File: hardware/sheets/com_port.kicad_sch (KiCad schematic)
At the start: 19 parts, among them J1 DE9_Pins, J2 Conn_01x03, J3 Conn_01x04, U1 16550, U2 MAX3241, U3 74HCT04, U4 74HCT08, U5 74HCT08, U6 74HCT125, Y1 1.8432MHz

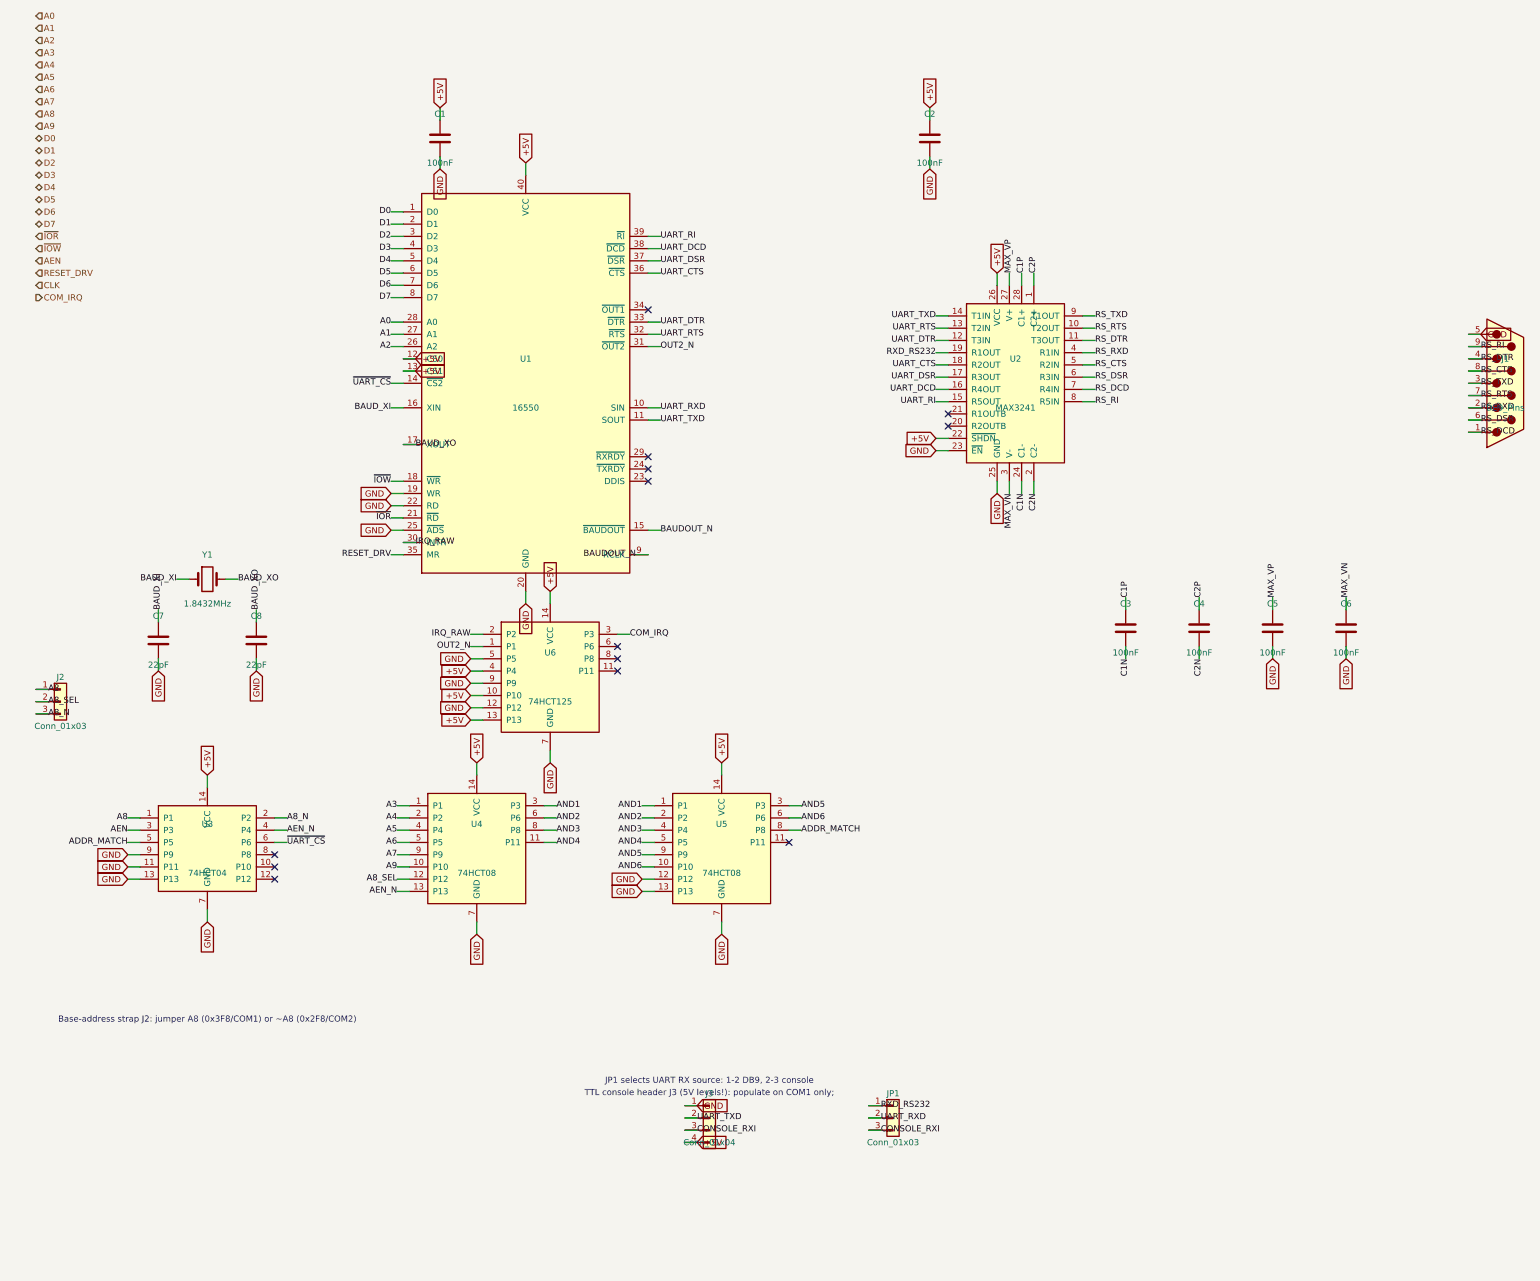
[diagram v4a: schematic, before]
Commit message: Design review 2026-07-11: rail protection, decoupling, wiring fixes
Protection:
- Sidecar +5V now feeds through a 2A polyfuse into +5V_ISA with an
  SMBJ5.0A clamp + 22uF bulk (a faulted ISA card trips its own fuse
  instead of dropping the board; back-fed voltage is clamped).
- USB-C VBUS enters through a 3A polyfuse with an SMBJ5.0A on +5V
  (backstop for the CFG1 9-20V failure mode). CH224K gains a 1uF VDD
  cap; its PG routes to Supervisor GPIO16 as PD_PG. Buck output
  doubled to 2x22uF, 10uF at VIN, extra rail bulk.
- Supervisor USB-A host port: 27R series termination (RP2040
  requirement), USBLC6-2SC6 ESD array, 100uF VBUS bulk.
- Video: HDMI +5V fused (500mA), HPD sensed on GPIO41, 100R series on
  VGA sync. TMDS ESD array deferred to layout (no symbol).
- card_isatest: V5RAW bulk, Q1 gate soft-start cap, TVS on DUT rail.

Wiring fixes:
- SPKR had no driver anywhere (netlist: 1 node). Bus MCU GPIO22
  reassigned from the diagnostics-only bus-CLK sense to SPKR; bus_mcu
  drops CLK from its interface. Doc 5.2 updated.
- bus_mcu C8 decoupled +3V3, a rail that sheet never uses -> 3V3_BUS.
- Storage IRQ5 was push-pull (permanently driven when idle) -> 2N7002
  + gated '125 tri-state, same convention as the LPT IRQ7 stage.
- MAX3241 pump caps resized to the 5V datasheet values (47nF/330nF).
- LPT DB25 status inputs get 4.7k pull-ups (floated with no printer).
- Audio line-out gets a 100R series isolator before the jack.

Best practices:
- Decoupling to ~1x100nF per IC on every sheet + bulk per board
  (cpu_core 7->16 incl. the naked 3.3V oscillator, storage 4->11,
  parallel 6->13, rtc/com/video/bus_mcu/card_isatest similar).
- All floating spare CMOS inputs tied ('00/'74/'157/'02/'04/'125
  sections across cpu_core, bus_mcu, rtc, storage, card_isatest).

Sourcing: new parts mapped in parts.py with JLC-verified LCSC numbers;
Power_Protection lib registered in the tools; TPS563200 stock alert
(4 pcs left at JLC) flagged in parts.py + jlcpcb-sourcing.md. All
decisi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
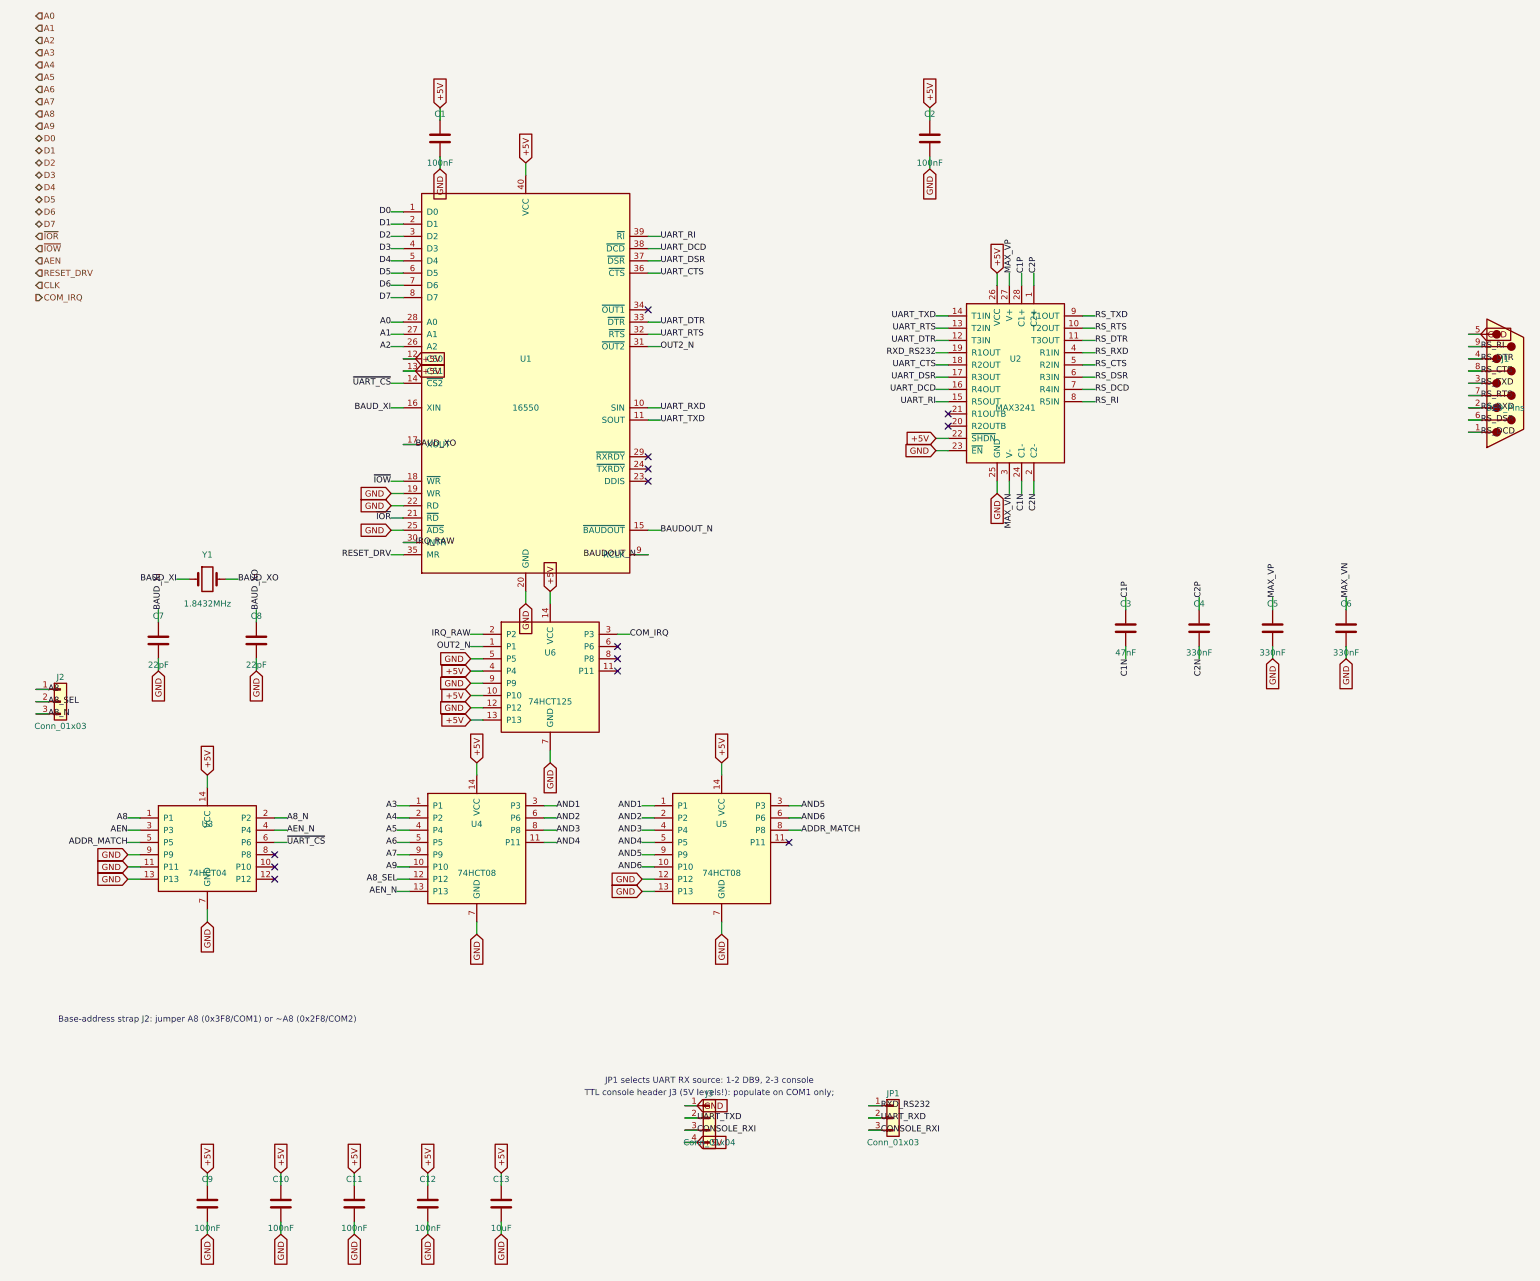
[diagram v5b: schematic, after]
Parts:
- added C10, C11, C12, C9: 100nF, symbol Device:C
- added C13: 10uF, symbol Device:C
- C3: value 100nF -> 47nF; LCSC Part Num C14663 -> C1622
- C4, C5, C6: value 100nF -> 330nF; LCSC Part Num C14663 -> C1615
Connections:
- net +5V: now also C10.1, C11.1, C12.1, C13.1, C9.1
- net GND: now also C10.2, C11.2, C12.2, C13.2, C9.2

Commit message: COM/LPT: on-board enable jumpers + base-addr/IRQ straps
The motherboard's COM1/COM2 IRQs were hard-wired at build time (INSTANCES
net remap); the LPT port had no strap or disable at all. Both sheets now
carry the full jumper set a real card would have, so an on-board port can
be disabled or re-strapped to make room for the same peripheral on the
sidecar chain:

- com_port: JP3 enable gates the 16550's spare active-high CS1 (open =
  never selected; IRQ needs no gating since MCR resets to 0 -> OUT2# high
  -> '125 released). JP2 picks IRQ4/IRQ3 (open = polled) on the sheet, so
  the sheet now exports IRQ3+IRQ4 and the INSTANCES remap is gone -- both
  instances share the lines safely (tri-state). J2 base strap unchanged.
- parallel: JP1 base 0x378/0x278 (differ only in A8; a spare U12 NAND
  makes ~A8), JP2 enable lifts the register-select '138's spare ~E1 (open
  kills every select, read enable and latch clock), JP3 IRQ7/IRQ5 (open =
  polled; IRQ5 noted as conflicting with the storage card if both enabled).
  PINS now export IRQ5+IRQ7.
- parts.py: Conn_01x02 breakaway-header fallback for the 2-pin jumpers.

Downstream sheet .kicad_sch diffs are instance-path UUID shifts from the
grown com_port/parallel interfaces (deterministic counter), not edits.

Verified: netlist shows IRQ3/IRQ4 spanning sidecar + both COM straps + the
Bus MCU collector; IRQ5 spans sidecar + LPT strap + storage + collector;
each enable net ties jumper + pull resistor + chip-select pin. Zero
structural ERC on motherboard and cards.

Co-Authored-By: Claude Fable 5 <noreply@anthropic.com>
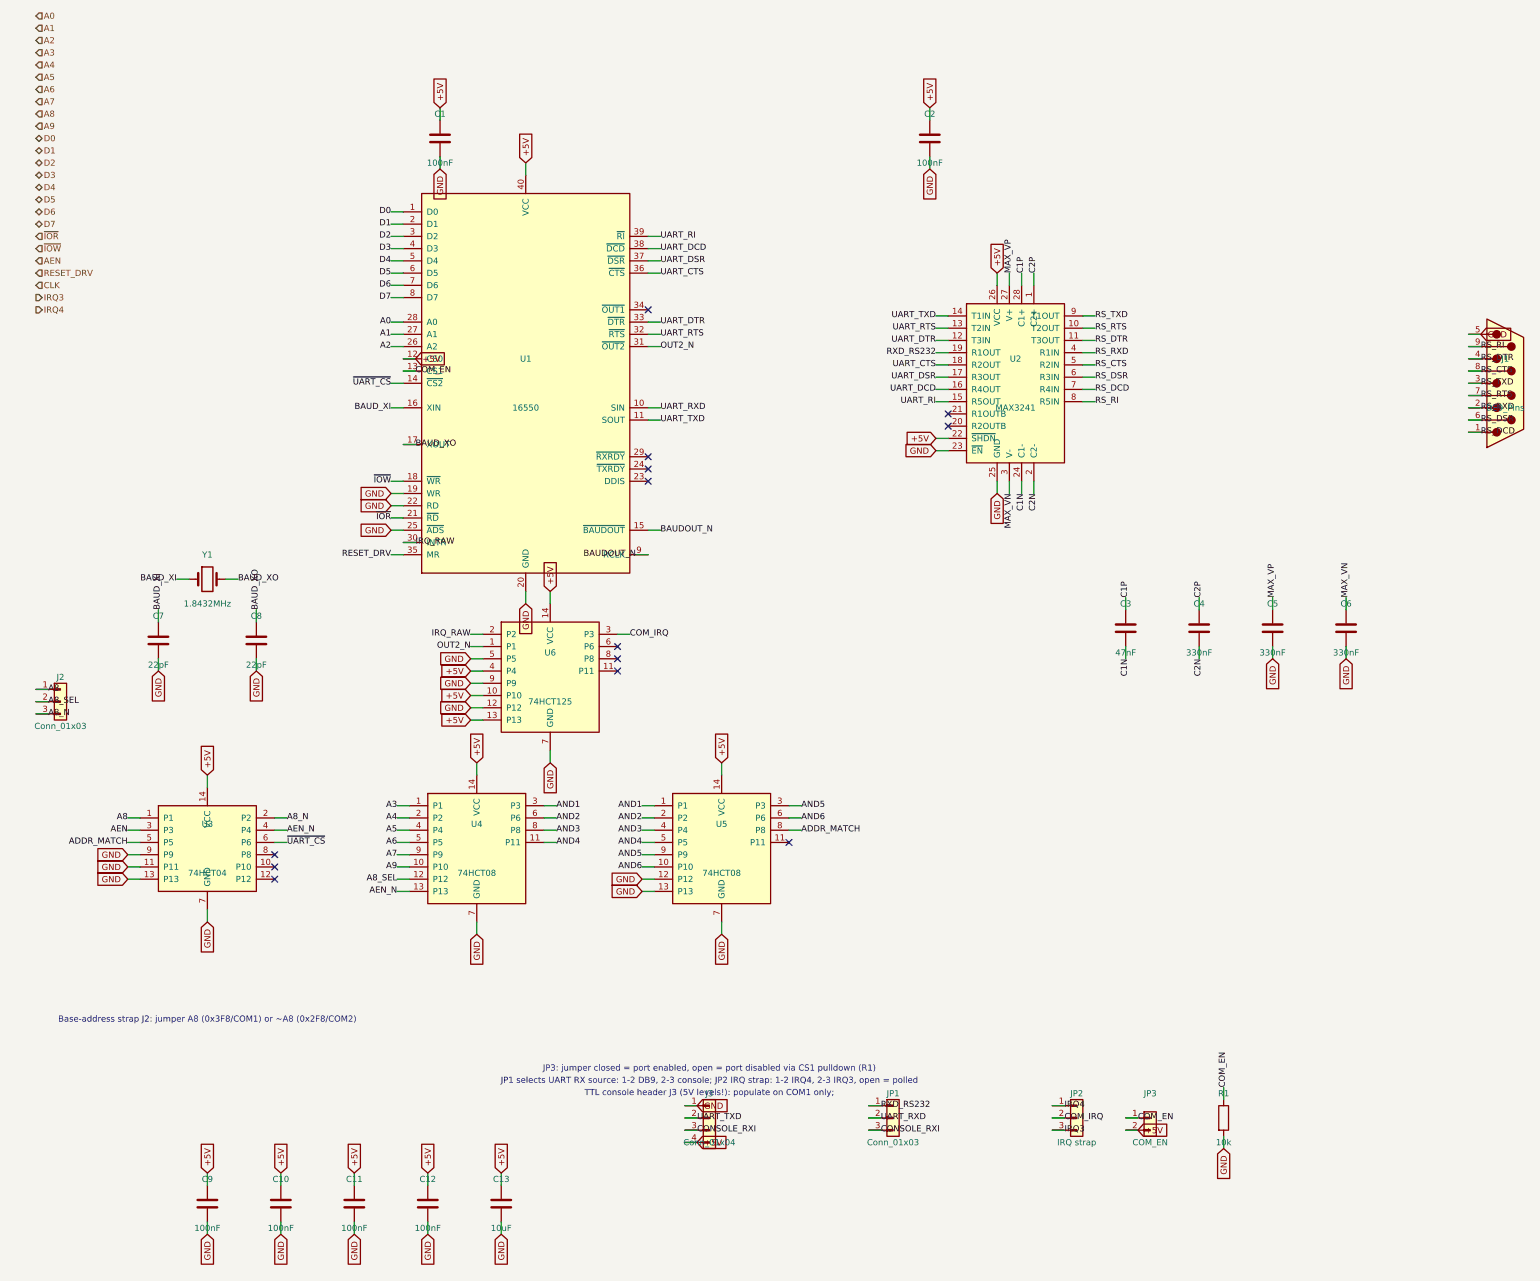
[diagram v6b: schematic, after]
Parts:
- added JP2: IRQ strap, symbol Connector_Generic:Conn_01x03
- added JP3: COM_EN, symbol Connector_Generic:Conn_01x02
- added R1: 10k, symbol Device:R
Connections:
- net +5V: now also JP3.2 (Pin_2); no longer U1.13 (CS1)
- net COM_IRQ: now also JP2.2 (Pin_2)
- net GND: now also R1.2
- new net COM_EN: JP3.1 (Pin_1), R1.1, U1.13 (CS1)
- new net IRQ3: JP2.3 (Pin_3)
- new net IRQ4: JP2.1 (Pin_1)
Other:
- note added: "JP1 selects UART RX source: 1-2 DB9, 2-3 console; JP2 IRQ strap: 1-2 IRQ4, 2-3 IRQ3, open = polled"
- note added: "JP3: jumper closed = port enabled, open = port disabled via CS1 pulldown (R1)"
- note removed: "JP1 selects UART RX source: 1-2 DB9, 2-3 console"
